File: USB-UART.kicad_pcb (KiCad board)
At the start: 2 copper layers, 44.8 x 24 mm, 22 parts, among them CON1 USB-MICRO-B, P1 CONN_01X03, P2 CONN_01X06, P3 CONN_01X01, U1 FT232RL, U2 ADuM5010-DC/DC-150mW-SSOP20-I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, U3 ADuM3211, U4 ADuM5010-DC/DC-150mW-SSOP20-I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, U5 ADuM3211

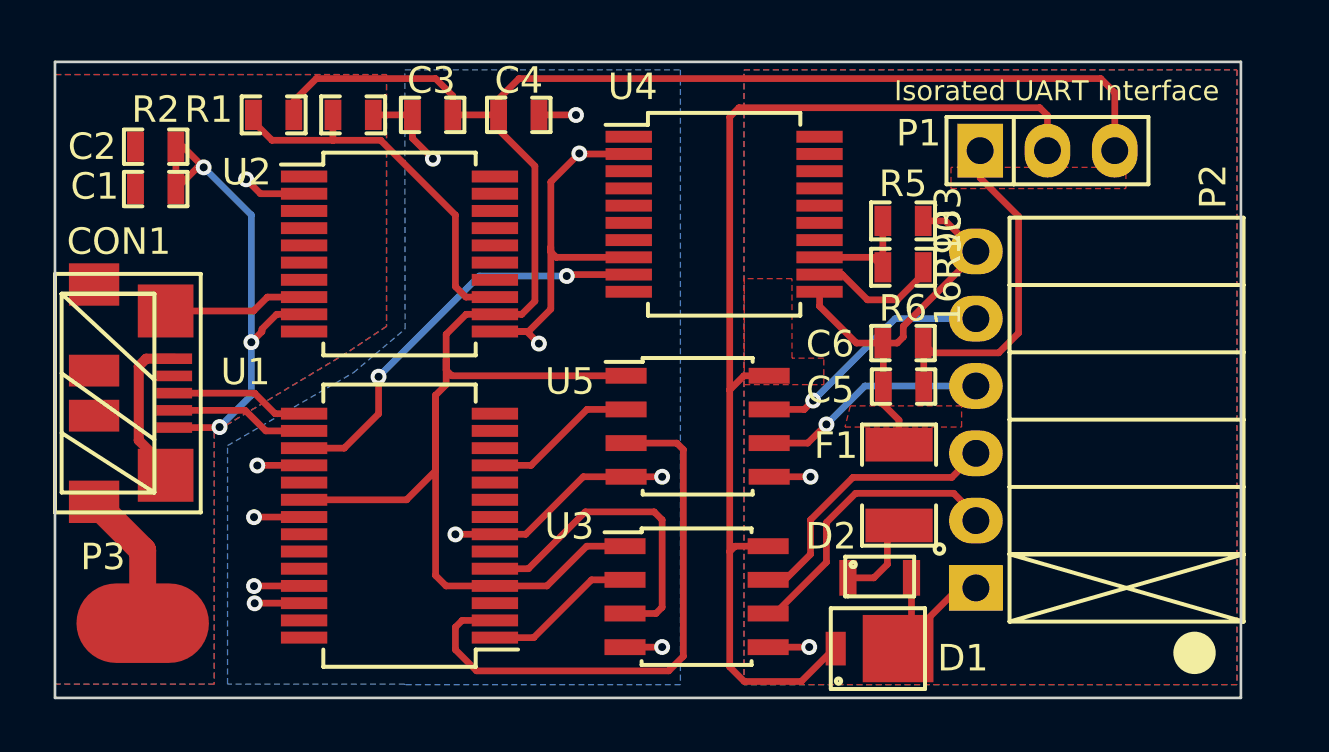
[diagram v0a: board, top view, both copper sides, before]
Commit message: Dress to ground.
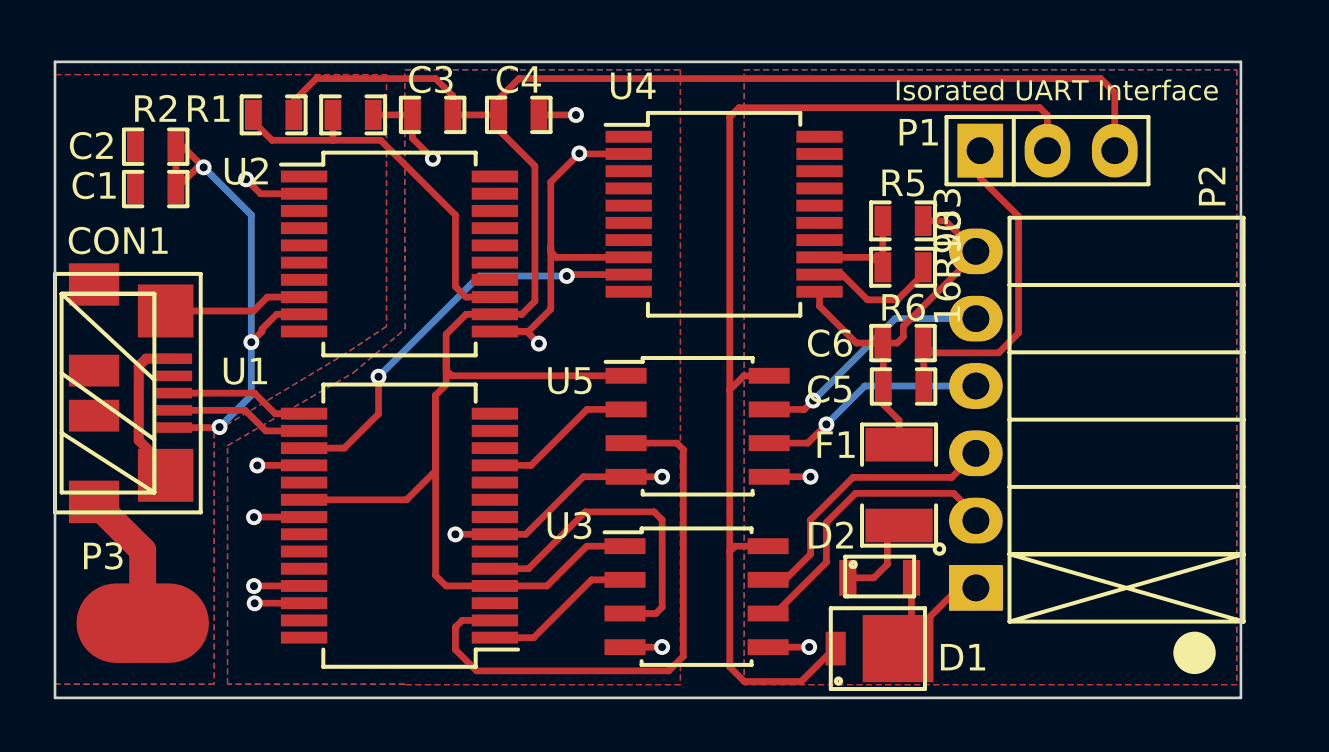
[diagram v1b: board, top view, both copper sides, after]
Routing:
- added copper zone on F.Cu, net GNDA

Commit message: Change to wire
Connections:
- U1 pad 1: Net-(U2-Pad1) -> Net-(U1-Pad1)
- U1 pad 5: Net-(U2-Pad5) -> Net-(U1-Pad5)
- U3 pad 2: Net-(U2-Pad1) -> Net-(U1-Pad5)
- U3 pad 3: Net-(U2-Pad5) -> Net-(U1-Pad1)
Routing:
- net Net-(U2-Pad5): track 12.1 -> 0.00 mm
- net Net-(U1-Pad5): track 0.00 -> 10.7 mm
- net Net-(U2-Pad1): track 5.81 -> 0.00 mm
- net Net-(U1-Pad1): track 0.00 -> 5.29 mm
- removed copper zone on F.Cu, net GNDA
